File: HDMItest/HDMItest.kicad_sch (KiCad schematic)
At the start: 4 parts, among them J1 HDMI_A, J2 Conn_02x06_Odd_Even

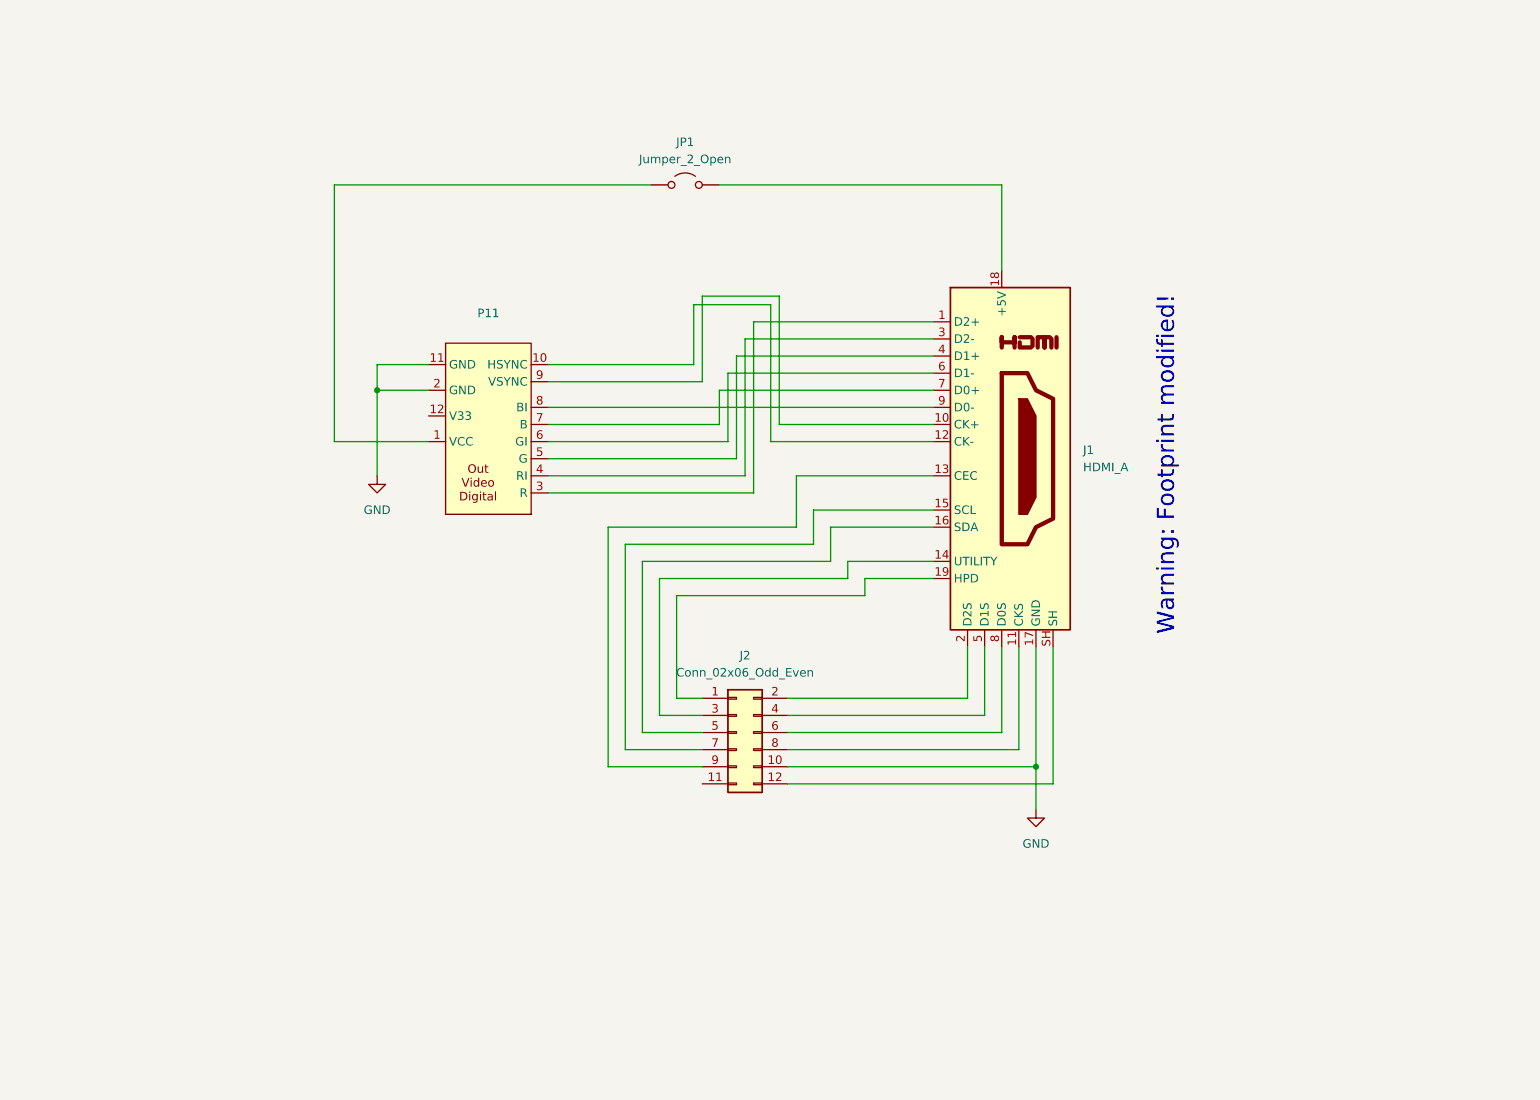
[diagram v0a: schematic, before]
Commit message: new HDMI test with re-driver
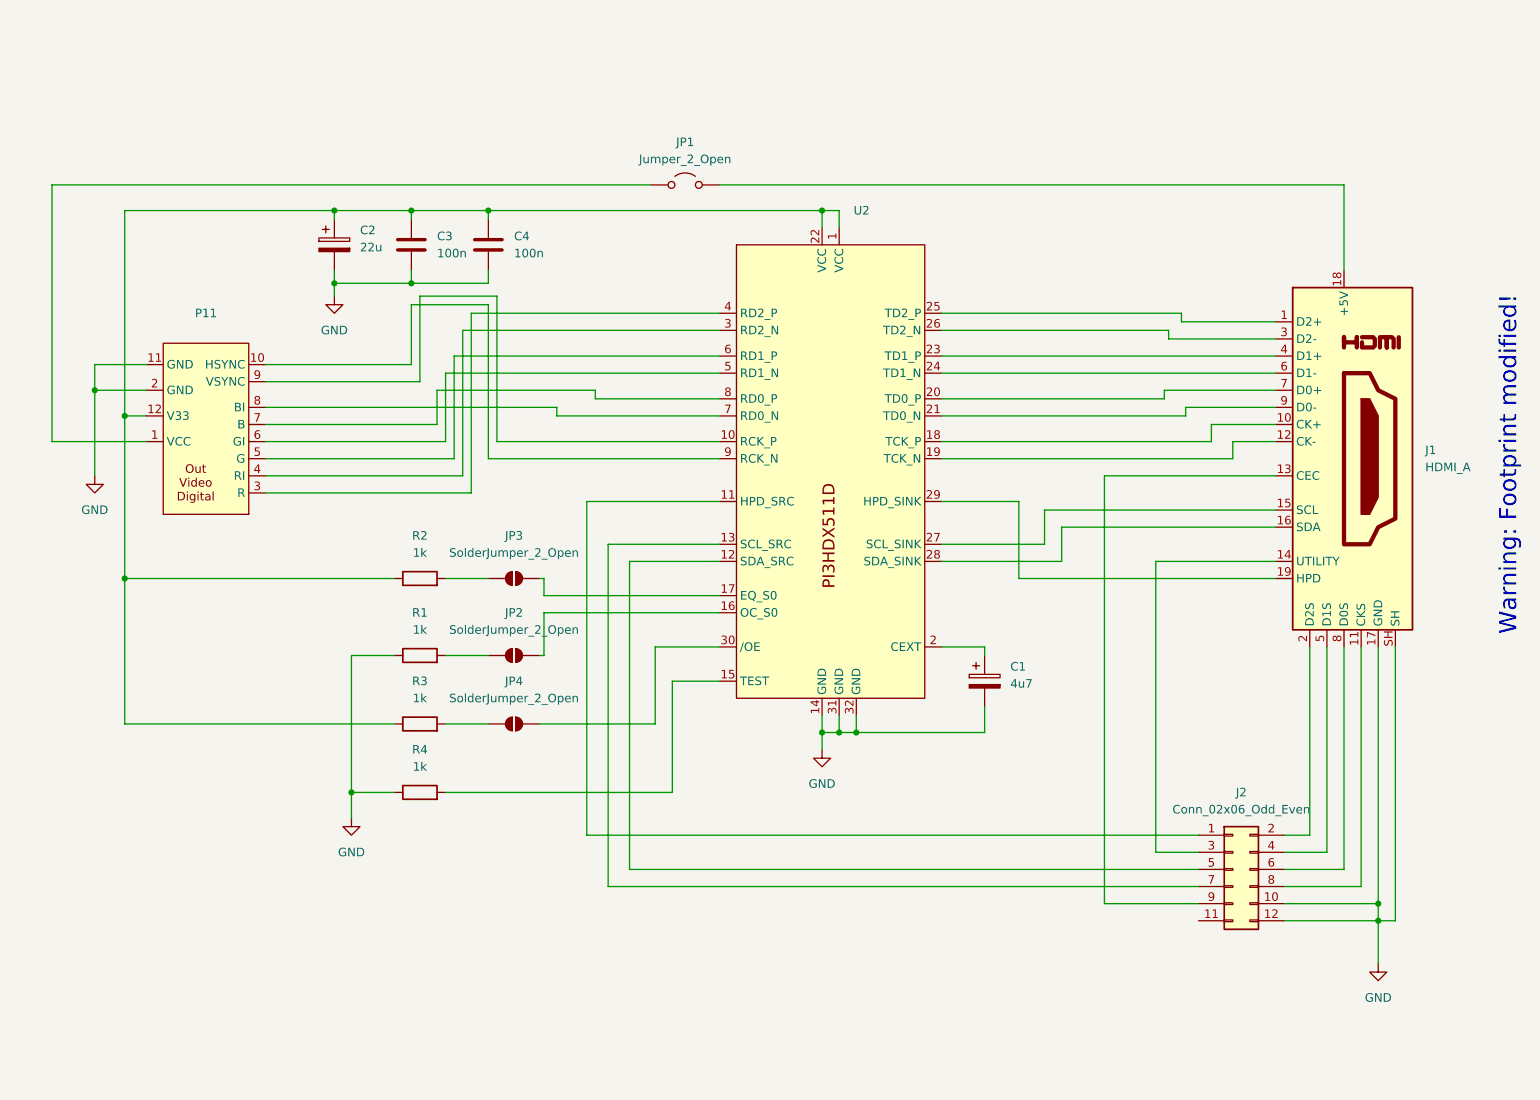
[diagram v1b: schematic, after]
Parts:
- added C1: 4u7, Capacitor_SMD:C_0805_2012Metric_Pad1.18x1.45mm_HandSolder, symbol Device:C_Polarized
- added C2: 22u, Capacitor_SMD:C_0805_2012Metric_Pad1.18x1.45mm_HandSolder, symbol Device:C_Polarized
- added C3, C4: 100n, Capacitor_SMD:C_0603_1608Metric_Pad1.08x0.95mm_HandSolder, symbol Device:C
- added JP2, JP3, JP4: SolderJumper_2_Open, Jumper:SolderJumper-2_P1.3mm_Open_RoundedPad1.0x1.5mm, symbol Jumper:SolderJumper_2_Open
- added R1, R2, R3, R4: 1k, Resistor_SMD:R_0603_1608Metric_Pad0.98x0.95mm_HandSolder, symbol Device:R
- added U2: ~, Package_DFN_QFN:Diodes_ZL32_TQFN-32-1EP_3x6mm_P0.4mm_EP1.25x3.5mm, symbol HDMI:PI3HDX511Z
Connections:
- net GND: now also J1.SH, J2.12 (Pin_12), C1.2, C2.2, C3.2, C4.2, R1.1, R4.1, U2.14 (GND), U2.31 (GND), U2.32 (GND)
- net at J2.1 (Pin_1): now also U2.11 (HPD_SRC); no longer J1.19 (HPD)
- net at J2.5 (Pin_5): now also U2.12 (SDA_SRC); no longer J1.16 (SDA)
- net at J2.7 (Pin_7): now also U2.13 (SCL_SRC); no longer J1.15 (SCL)
- net at P11.10 (HSYNC): now also U2.9 (RCK_N); no longer J1.12 (CK-)
- net at P11.12 (V33): now also C2.1, C3.1, C4.1, R2.1, R3.1, U2.1 (VCC), U2.22 (VCC)
- net at P11.3 (R): now also U2.4 (RD2_P); no longer J1.1 (D2+)
- net at P11.4 (RI): now also U2.3 (RD2_N); no longer J1.3 (D2-)
- net at P11.5 (G): now also U2.6 (RD1_P); no longer J1.4 (D1+)
- net at P11.6 (GI): now also U2.5 (RD1_N); no longer J1.6 (D1-)
- net at P11.7 (B): now also U2.8 (RD0_P); no longer J1.7 (D0+)
- net at P11.8 (BI): now also U2.7 (RD0_N); no longer J1.9 (D0-)
- net at P11.9 (VSYNC): now also U2.10 (RCK_P); no longer J1.10 (CK+)
- new net: JP4.1 (A), R3.2
- new net: C1.1, U2.2 (CEXT)
- new net: R4.2, U2.15 (TEST)
- new net: JP3.1 (A), R2.2
- new net: JP3.2 (B), U2.17 (EQ_S0)
- new net: JP2.1 (A), R1.2
- new net: JP2.2 (B), U2.16 (OC_S0)
- new net: J1.1 (D2+), U2.25 (TD2_P)
- new net: J1.10 (CK+), U2.18 (TCK_P)
- new net: J1.12 (CK-), U2.19 (TCK_N)
- new net: J1.15 (SCL), U2.27 (SCL_SINK)
- new net: J1.16 (SDA), U2.28 (SDA_SINK)
- new net: J1.19 (HPD), U2.29 (HPD_SINK)
- new net: J1.3 (D2-), U2.26 (TD2_N)
- new net: J1.4 (D1+), U2.23 (TD1_P)
- new net: J1.6 (D1-), U2.24 (TD1_N)
- new net: J1.7 (D0+), U2.20 (TD0_P)
- new net: J1.9 (D0-), U2.21 (TD0_N)
- new net: JP4.2 (B), U2.30 (/OE)
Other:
- moved on the sheet: J1, J2, P11

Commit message: new HDMI adapter with AC coupling
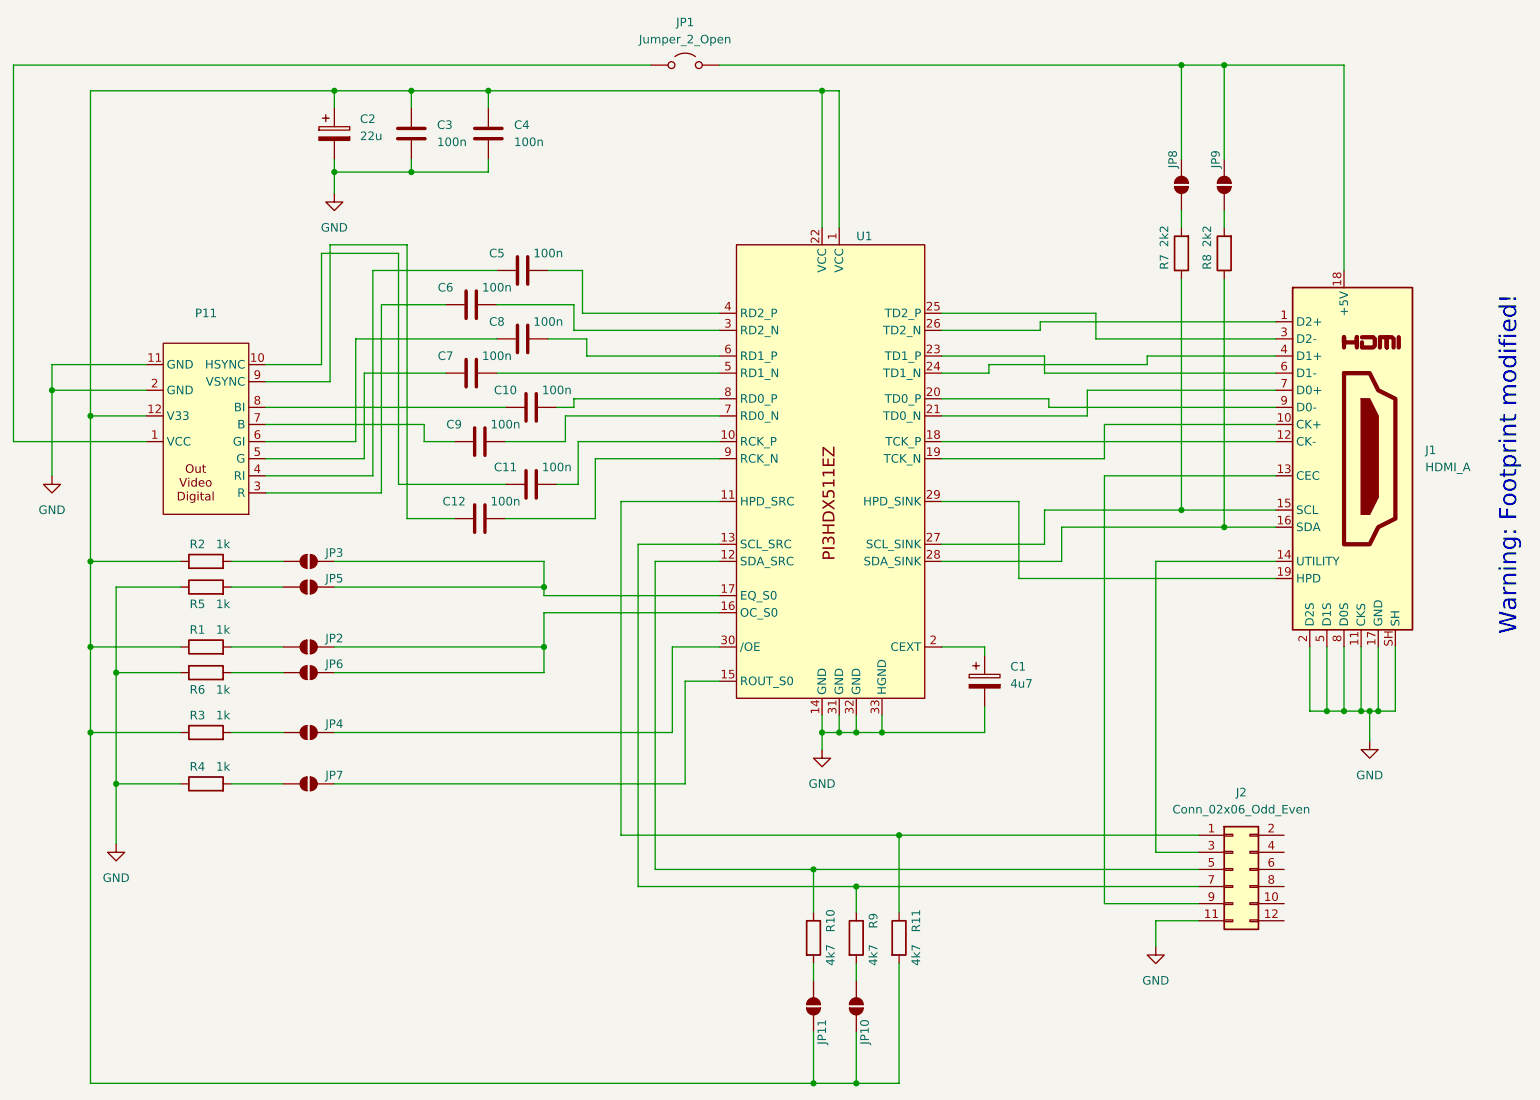
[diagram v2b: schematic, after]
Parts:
- removed U2: ~, Package_DFN_QFN:Diodes_ZL32_TQFN-32-1EP_3x6mm_P0.4mm_EP1.25x3.5mm, symbol HDMI:PI3HDX511Z
- added C10, C11, C12, C5, C6, C7, C8, C9: 100n, Capacitor_SMD:C_0603_1608Metric_Pad1.08x0.95mm_HandSolder, symbol Device:C
- added JP10, JP11, JP5, JP6, JP7, JP8, JP9: SolderJumper_2_Open, Jumper:SolderJumper-2_P1.3mm_Open_RoundedPad1.0x1.5mm, symbol Jumper:SolderJumper_2_Open
- added R10, R11, R9: 4k7, Resistor_SMD:R_0603_1608Metric_Pad0.98x0.95mm_HandSolder, symbol Device:R
- added R5, R6: 1k, Resistor_SMD:R_0603_1608Metric_Pad0.98x0.95mm_HandSolder, symbol Device:R
- added R7, R8: 2k2, Resistor_SMD:R_0603_1608Metric_Pad0.98x0.95mm_HandSolder, symbol Device:R
- added U1: ~, Package_DFN_QFN:Diodes_ZL32_TQFN-32-1EP_3x6mm_P0.4mm_EP1.25x3.5mm, symbol HDMI:PI3HDX511EZ
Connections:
- net GND: now also J1.11 (CKS), J1.2 (D2S), J1.5 (D1S), J1.8 (D0S), J2.11 (Pin_11), R5.1, R6.1, U1.14 (GND), U1.31 (GND), U1.32 (GND), U1.33 (HGND); no longer J2.10 (Pin_10), J2.12 (Pin_12), R1.1
- net at C2.1, C3.1, C4.1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: now also R1.1, JP10.2 (B), JP11.2 (B), R11.2, U1.1 (VCC), U1.22 (VCC)
- net at J2.1 (Pin_1): now also R11.1, U1.11 (HPD_SRC)
- net at J2.2 (Pin_2): no longer J1.2 (D2S)
- net at J2.4 (Pin_4): no longer J1.5 (D1S)
- net at J2.5 (Pin_5): now also R10.1, U1.12 (SDA_SRC)
- net at J2.6 (Pin_6): no longer J1.8 (D0S)
- net at J2.7 (Pin_7): now also R9.1, U1.13 (SCL_SRC)
- net at J2.8 (Pin_8): no longer J1.11 (CKS)
- net at P11.10 (HSYNC): now also C11.1
- net at P11.3 (R): now also C6.1
- net at P11.4 (RI): now also C5.1
- net at P11.5 (G): now also C7.1
- net at P11.6 (GI): now also C8.1
- net at P11.7 (B): now also C9.1
- net at P11.8 (BI): now also C10.1
- net at P11.9 (VSYNC): now also C12.1
- net at C1.1: now also U1.2 (CEXT)
- net at R4.2: now also JP7.1 (A)
- net at JP3.2 (B): now also JP5.2 (B), U1.17 (EQ_S0)
- net at J1.18 (+5V), JP1.2 (B): now also JP8.2 (B), JP9.2 (B)
- net at JP2.2 (B): now also JP6.2 (B), U1.16 (OC_S0)
- net at J1.1 (D2+): now also U1.26 (TD2_N)
- net at J1.10 (CK+): now also U1.19 (TCK_N)
- net at J1.12 (CK-): now also U1.18 (TCK_P)
- net at J1.15 (SCL): now also R7.1, U1.27 (SCL_SINK)
- net at J1.16 (SDA): now also R8.1, U1.28 (SDA_SINK)
- net at J1.19 (HPD): now also U1.29 (HPD_SINK)
- net at J1.3 (D2-): now also U1.25 (TD2_P)
- net at J1.4 (D1+): now also U1.24 (TD1_N)
- net at J1.6 (D1-): now also U1.23 (TD1_P)
- net at J1.7 (D0+): now also U1.21 (TD0_N)
- net at J1.9 (D0-): now also U1.20 (TD0_P)
- net at JP4.2 (B): now also U1.30 (/OE)
- new net: C5.2, U1.4 (RD2_P)
- new net: C10.2, U1.8 (RD0_P)
- new net: JP6.1 (A), R6.2
- new net: JP11.1 (A), R10.2
- new net: C6.2, U1.3 (RD2_N)
- new net: JP7.2 (B), U1.15 (ROUT_S0)
- new net: C7.2, U1.5 (RD1_N)
- new net: C11.2, U1.10 (RCK_P)
- new net: JP8.1 (A), R7.2
- new net: C8.2, U1.6 (RD1_P)
- new net: C9.2, U1.7 (RD0_N)
- new net: C12.2, U1.9 (RCK_N)
- new net: JP9.1 (A), R8.2
- new net: JP10.1 (A), R9.2
- new net: JP5.1 (A), R5.2
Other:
- moved on the sheet: C2, C3, C4, JP1, JP2, JP3, JP4, R1, R2, R3, R4
